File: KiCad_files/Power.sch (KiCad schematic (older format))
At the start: 101 parts, among them J2 PCIe_6_Pin_Power, Q1 Q_NMOS_DGS, Q2 Q_PMOS_DGS, U1 XC7A35T_CSG325, U13 LM2676, U2 MAX15027, U3 PI3420, U4 PI3421, U5 PI3420

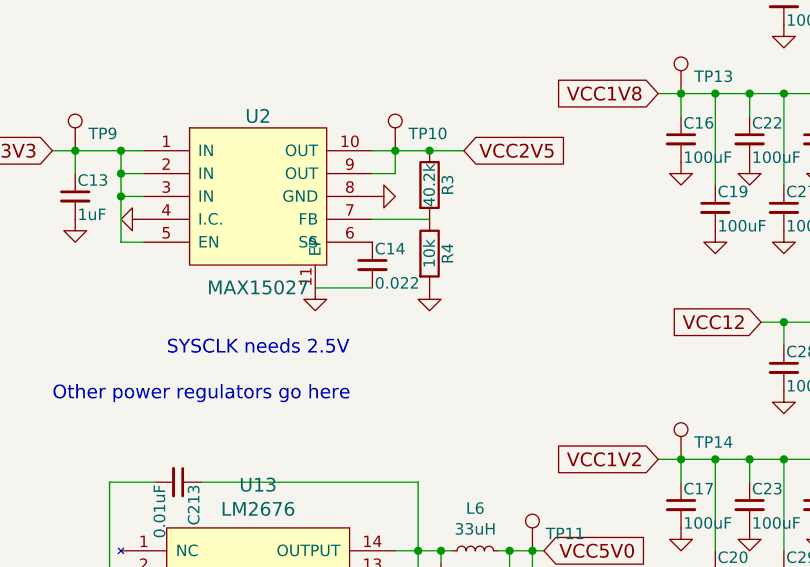
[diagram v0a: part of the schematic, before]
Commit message: Started mapping footprints
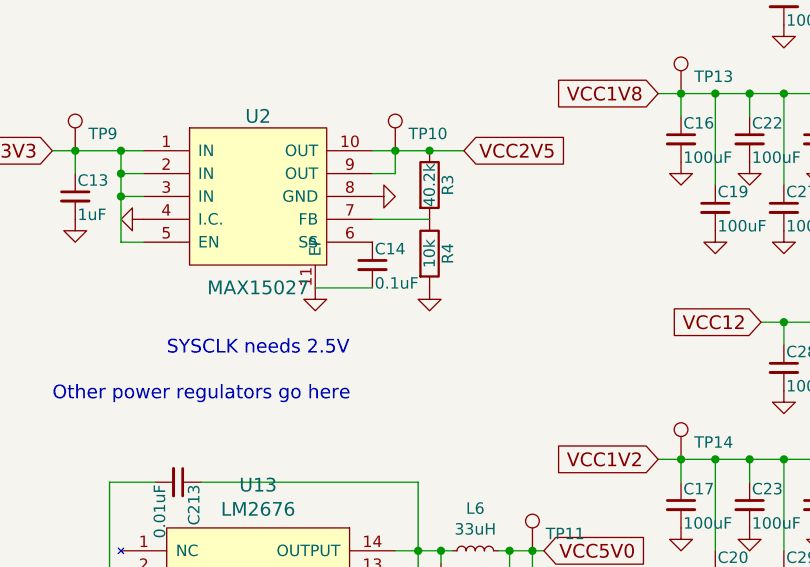
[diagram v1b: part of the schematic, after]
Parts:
- C11, C33, C35, C42, C43, C48, C49, C54, C56, C63, C64, C66, C67: footprint (none) -> Capacitors_SMD:C_0805
- C12, C15, C16, C17, C18, C19, C20, C21, C22, C23, C24, C25, C26, C27, C28, C29, C30, C31, C32, C34: footprint (none) -> Capacitors_SMD:C_1210
- C13: footprint (none) -> Capacitors_SMD:C_0402
- C14: value 0.022 -> 0.1uF; footprint (none) -> Capacitors_SMD:C_0402
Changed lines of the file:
@@
 F 0 "C11" H 2125 1350 50  0000 L CNN
 F 1 "10uF" H 2125 1150 50  0000 L CNN
-F 2 "" H 2138 1100 50  0001 C CNN
+F 2 "Capacitors_SMD:C_0805" H 2138 1100 50  0001 C CNN
 F 3 "" H 2100 1250 50  0001 C CNN
 	1    2100 1250
@@
 F 0 "C12" H 2475 1350 50  0000 L CNN
 F 1 "330uF" H 2475 1150 50  0000 L CNN
-F 2 "" H 2450 1250 50  0001 C CNN
+F 2 "Capacitors_SMD:C_1210" H 2450 1250 50  0001 C CNN
 F 3 "" H 2450 1250 50  0001 C CNN
 	1    2450 1250
@@
 F 0 "C15" H 6760 1870 50  0000 L CNN
 F 1 "100uF" H 6760 1720 50  0000 L CNN
-F 2 "" H 6750 1800 50  0001 C CNN
+F 2 "Capacitors_SMD:C_1210" H 6750 1800 50  0001 C CNN
 F 3 "" H 6750 1800 50  0001 C CNN
 	1    6750 1800
@@
 F 0 "C24" H 7210 1270 50  0000 L CNN
 F 1 "100uF" H 7210 1120 50  0000 L CNN
-F 2 "" H 7200 1200 50  0001 C CNN
+F 2 "Capacitors_SMD:C_1210" H 7200 1200 50  0001 C CNN
 F 3 "" H 7200 1200 50  0001 C CNN
 	1    7200 1200
@@
 F 0 "C33" H 7510 1270 50  0000 L CNN
 F 1 "22uF" H 7510 1120 50  0000 L CNN
-F 2 "" H 7500 1200 50  0001 C CNN
+F 2 "Capacitors_SMD:C_0805" H 7500 1200 50  0001 C CNN
 F 3 "" H 7500 1200 50  0001 C CNN
 	1    7500 1200
@@
 F 0 "C42" H 7710 1270 50  0000 L CNN
 F 1 "22uF" H 7710 1120 50  0000 L CNN
-F 2 "" H 7700 1200 50  0001 C CNN
+F 2 "Capacitors_SMD:C_0805" H 7700 1200 50  0001 C CNN
 F 3 "" H 7700 1200 50  0001 C CNN
 	1    7700 1200
@@
 F 0 "C48" H 7910 1270 50  0000 L CNN
 F 1 "22uF" H 7910 1120 50  0000 L CNN
-F 2 "" H 7900 1200 50  0001 C CNN
+F 2 "Capacitors_SMD:C_0805" H 7900 1200 50  0001 C CNN
 F 3 "" H 7900 1200 50  0001 C CNN
 	1    7900 1200
@@
 F 0 "C54" H 8110 1270 50  0000 L CNN
 F 1 "22uF" H 8110 1120 50  0000 L CNN
-F 2 "" H 8100 1200 50  0001 C CNN
+F 2 "Capacitors_SMD:C_0805" H 8100 1200 50  0001 C CNN
 F 3 "" H 8100 1200 50  0001 C CNN
 	1    8100 1200
@@
 F 0 "C63" H 8310 1270 50  0000 L CNN
 F 1 "22uF" H 8310 1120 50  0000 L CNN
-F 2 "" H 8300 1200 50  0001 C CNN
+F 2 "Capacitors_SMD:C_0805" H 8300 1200 50  0001 C CNN
 F 3 "" H 8300 1200 50  0001 C CNN
 	1    8300 1200
@@
 F 0 "C66" H 8510 1270 50  0000 L CNN
 F 1 "22uF" H 8510 1120 50  0000 L CNN
-F 2 "" H 8500 1200 50  0001 C CNN
+F 2 "Capacitors_SMD:C_0805" H 8500 1200 50  0001 C CNN
 F 3 "" H 8500 1200 50  0001 C CNN
 	1    8500 1200
@@
 F 0 "C18" H 6910 2170 50  0000 L CNN
 F 1 "100uF" H 6910 2020 50  0000 L CNN
-F 2 "" H 6900 2100 50  0001 C CNN
+F 2 "Capacitors_SMD:C_1210" H 6900 2100 50  0001 C CNN
 F 3 "" H 6900 2100 50  0001 C CNN
 	1    6900 2100
@@
 F 0 "C21" H 7060 1870 50  0000 L CNN
 F 1 "100uF" H 7060 1720 50  0000 L CNN
-F 2 "" H 7050 1800 50  0001 C CNN
+F 2 "Capacitors_SMD:C_1210" H 7050 1800 50  0001 C CNN
 F 3 "" H 7050 1800 50  0001 C CNN
 	1    7050 1800
@@
 F 0 "C25" H 7210 2170 50  0000 L CNN
 F 1 "100uF" H 7210 2020 50  0000 L CNN
-F 2 "" H 7200 2100 50  0001 C CNN
+F 2 "Capacitors_SMD:C_1210" H 7200 2100 50  0001 C CNN
 F 3 "" H 7200 2100 50  0001 C CNN
 	1    7200 2100
@@
 F 0 "C30" H 7360 1870 50  0000 L CNN
 F 1 "100uF" H 7360 1720 50  0000 L CNN
-F 2 "" H 7350 1800 50  0001 C CNN
+F 2 "Capacitors_SMD:C_1210" H 7350 1800 50  0001 C CNN
 F 3 "" H 7350 1800 50  0001 C CNN
 	1    7350 1800
@@
 F 0 "C34" H 7510 2170 50  0000 L CNN
 F 1 "100uF" H 7510 2020 50  0000 L CNN
-F 2 "" H 7500 2100 50  0001 C CNN
+F 2 "Capacitors_SMD:C_1210" H 7500 2100 50  0001 C CNN
 F 3 "" H 7500 2100 50  0001 C CNN
 	1    7500 2100
@@
 F 0 "C16" H 6760 3470 50  0000 L CNN
 F 1 "100uF" H 6760 3320 50  0000 L CNN
-F 2 "" H 6750 3400 50  0001 C CNN
+F 2 "Capacitors_SMD:C_1210" H 6750 3400 50  0001 C CNN
 F 3 "" H 6750 3400 50  0001 C CNN
 	1    6750 3400
@@
 F 0 "C26" H 7210 2870 50  0000 L CNN
 F 1 "100uF" H 7210 2720 50  0000 L CNN
-F 2 "" H 7200 2800 50  0001 C CNN
+F 2 "Capacitors_SMD:C_1210" H 7200 2800 50  0001 C CNN
 F 3 "" H 7200 2800 50  0001 C CNN
 	1    7200 2800
@@
 F 0 "C35" H 7510 2870 50  0000 L CNN
 F 1 "22uF" H 7510 2720 50  0000 L CNN
-F 2 "" H 7500 2800 50  0001 C CNN
+F 2 "Capacitors_SMD:C_0805" H 7500 2800 50  0001 C CNN
 F 3 "" H 7500 2800 50  0001 C CNN
 	1    7500 2800
@@
 F 0 "C43" H 7710 2870 50  0000 L CNN
 F 1 "22uF" H 7710 2720 50  0000 L CNN
-F 2 "" H 7700 2800 50  0001 C CNN
+F 2 "Capacitors_SMD:C_0805" H 7700 2800 50  0001 C CNN
 F 3 "" H 7700 2800 50  0001 C CNN
 	1    7700 2800
@@
 F 0 "C49" H 7910 2870 50  0000 L CNN
 F 1 "22uF" H 7910 2720 50  0000 L CNN
-F 2 "" H 7900 2800 50  0001 C CNN
+F 2 "Capacitors_SMD:C_0805" H 7900 2800 50  0001 C CNN
 F 3 "" H 7900 2800 50  0001 C CNN
 	1    7900 2800
@@
 F 0 "C56" H 8110 2870 50  0000 L CNN
 F 1 "22uF" H 8110 2720 50  0000 L CNN
-F 2 "" H 8100 2800 50  0001 C CNN
+F 2 "Capacitors_SMD:C_0805" H 8100 2800 50  0001 C CNN
 F 3 "" H 8100 2800 50  0001 C CNN
 	1    8100 2800
@@
 F 0 "C64" H 8310 2870 50  0000 L CNN
 F 1 "22uF" H 8310 2720 50  0000 L CNN
-F 2 "" H 8300 2800 50  0001 C CNN
+F 2 "Capacitors_SMD:C_0805" H 8300 2800 50  0001 C CNN
 F 3 "" H 8300 2800 50  0001 C CNN
 	1    8300 2800
@@
 F 0 "C67" H 8510 2870 50  0000 L CNN
 F 1 "22uF" H 8510 2720 50  0000 L CNN
-F 2 "" H 8500 2800 50  0001 C CNN
+F 2 "Capacitors_SMD:C_0805" H 8500 2800 50  0001 C CNN
 F 3 "" H 8500 2800 50  0001 C CNN
 	1    8500 2800
@@
 F 0 "C19" H 6910 3770 50  0000 L CNN
 F 1 "100uF" H 6910 3620 50  0000 L CNN
-F 2 "" H 6900 3700 50  0001 C CNN
+F 2 "Capacitors_SMD:C_1210" H 6900 3700 50  0001 C CNN
 F 3 "" H 6900 3700 50  0001 C CNN
 	1    6900 3700
@@
 F 0 "C22" H 7060 3470 50  0000 L CNN
 F 1 "100uF" H 7060 3320 50  0000 L CNN
-F 2 "" H 7050 3400 50  0001 C CNN
+F 2 "Capacitors_SMD:C_1210" H 7050 3400 50  0001 C CNN
 F 3 "" H 7050 3400 50  0001 C CNN
 	1    7050 3400
@@
 F 0 "C27" H 7210 3770 50  0000 L CNN
 F 1 "100uF" H 7210 3620 50  0000 L CNN
-F 2 "" H 7200 3700 50  0001 C CNN
+F 2 "Capacitors_SMD:C_1210" H 7200 3700 50  0001 C CNN
 F 3 "" H 7200 3700 50  0001 C CNN
 	1    7200 3700
@@
 F 0 "C31" H 7360 3470 50  0000 L CNN
 F 1 "100uF" H 7360 3320 50  0000 L CNN
-F 2 "" H 7350 3400 50  0001 C CNN
+F 2 "Capacitors_SMD:C_1210" H 7350 3400 50  0001 C CNN
 F 3 "" H 7350 3400 50  0001 C CNN
 	1    7350 3400
@@
 F 0 "C17" H 6760 5070 50  0000 L CNN
 F 1 "100uF" H 6760 4920 50  0000 L CNN
-F 2 "" H 6750 5000 50  0001 C CNN
+F 2 "Capacitors_SMD:C_1210" H 6750 5000 50  0001 C CNN
 F 3 "" H 6750 5000 50  0001 C CNN
 	1    6750 5000
@@
 F 0 "C28" H 7210 4470 50  0000 L CNN
 F 1 "100uF" H 7210 4320 50  0000 L CNN
-F 2 "" H 7200 4400 50  0001 C CNN
+F 2 "Capacitors_SMD:C_1210" H 7200 4400 50  0001 C CNN
 F 3 "" H 7200 4400 50  0001 C CNN
 	1    7200 4400
@@
 F 0 "C20" H 6910 5370 50  0000 L CNN
 F 1 "100uF" H 6910 5220 50  0000 L CNN
-F 2 "" H 6900 5300 50  0001 C CNN
+F 2 "Capacitors_SMD:C_1210" H 6900 5300 50  0001 C CNN
 F 3 "" H 6900 5300 50  0001 C CNN
 	1    6900 5300
@@
 F 0 "C23" H 7060 5070 50  0000 L CNN
 F 1 "100uF" H 7060 4920 50  0000 L CNN
-F 2 "" H 7050 5000 50  0001 C CNN
+F 2 "Capacitors_SMD:C_1210" H 7050 5000 50  0001 C CNN
 F 3 "" H 7050 5000 50  0001 C CNN
 	1    7050 5000
@@
 F 0 "C29" H 7210 5370 50  0000 L CNN
 F 1 "100uF" H 7210 5220 50  0000 L CNN
-F 2 "" H 7200 5300 50  0001 C CNN
+F 2 "Capacitors_SMD:C_1210" H 7200 5300 50  0001 C CNN
 F 3 "" H 7200 5300 50  0001 C CNN
 	1    7200 5300
@@
 F 0 "C32" H 7360 5070 50  0000 L CNN
 F 1 "100uF" H 7360 4920 50  0000 L CNN
-F 2 "" H 7350 5000 50  0001 C CNN
+F 2 "Capacitors_SMD:C_1210" H 7350 5000 50  0001 C CNN
 F 3 "" H 7350 5000 50  0001 C CNN
 	1    7350 5000
@@
 F 0 "C13" H 4110 3720 50  0000 L CNN
 F 1 "1uF" H 4110 3570 50  0000 L CNN
-F 2 "" H 4100 3650 50  0001 C CNN
+F 2 "Capacitors_SMD:C_0402" H 4100 3650 50  0001 C CNN
 F 3 "" H 4100 3650 50  0001 C CNN
 	1    4100 3650
@@
 P 5400 3950
 F 0 "C14" H 5410 4020 50  0000 L CNN
-F 1 "0.022" H 5410 3870 50  0000 L CNN
-F 2 "" H 5400 3950 50  0001 C CNN
+F 1 "0.1uF" H 5410 3870 50  0000 L CNN
+F 2 "Capacitors_SMD:C_0402" H 5400 3950 50  0001 C CNN
 F 3 "" H 5400 3950 50  0001 C CNN
 	1    5400 3950

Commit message: Finished capacitor footprints
Total cost: ~$55
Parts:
- C210, C211, C36, C38, C39, C40, C41, C45, C46, C47: footprint (none) -> Capacitors_SMD:C_1210
- C212, C51, C52, C53, C55, C57, C59: footprint (none) -> Capacitors_SMD:C_0402
- C213, C60, C61, C62: footprint (none) -> Capacitors_SMD:C_0201
- C218: footprint (none) -> Capacitors_SMD:C_1206
- C37, C44, C50, C58, C65, C68: footprint (none) -> Capacitors_SMD:C_0805
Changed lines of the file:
@@
 F 0 "C51" H 7960 1870 50  0000 L CNN
 F 1 "1uF" H 7960 1720 50  0000 L CNN
-F 2 "" H 7950 1800 50  0001 C CNN
+F 2 "Capacitors_SMD:C_0402" H 7950 1800 50  0001 C CNN
 F 3 "" H 7950 1800 50  0001 C CNN
 	1    7950 1800
@@
 F 0 "C55" H 8110 1870 50  0000 L CNN
 F 1 "1uF" H 8110 1720 50  0000 L CNN
-F 2 "" H 8100 1800 50  0001 C CNN
+F 2 "Capacitors_SMD:C_0402" H 8100 1800 50  0001 C CNN
 F 3 "" H 8100 1800 50  0001 C CNN
 	1    8100 1800
@@
 F 0 "C39" H 7660 1870 50  0000 L CNN
 F 1 "100uF" H 7660 1720 50  0000 L CNN
-F 2 "" H 7650 1800 50  0001 C CNN
+F 2 "Capacitors_SMD:C_1210" H 7650 1800 50  0001 C CNN
 F 3 "" H 7650 1800 50  0001 C CNN
 	1    7650 1800
@@
 F 0 "C45" H 7810 2170 50  0000 L CNN
 F 1 "100uF" H 7810 2020 50  0000 L CNN
-F 2 "" H 7800 2100 50  0001 C CNN
+F 2 "Capacitors_SMD:C_1210" H 7800 2100 50  0001 C CNN
 F 3 "" H 7800 2100 50  0001 C CNN
 	1    7800 2100
@@
 F 0 "C60" H 8260 1870 50  0000 L CNN
 F 1 "0.1uF" H 8260 1720 50  0000 L CNN
-F 2 "" H 8250 1800 50  0001 C CNN
+F 2 "Capacitors_SMD:C_0201" H 8250 1800 50  0001 C CNN
 F 3 "" H 8250 1800 50  0001 C CNN
 	1    8250 1800
@@
 F 0 "C36" H 7510 3770 50  0000 L CNN
 F 1 "100uF" H 7510 3620 50  0000 L CNN
-F 2 "" H 7500 3700 50  0001 C CNN
+F 2 "Capacitors_SMD:C_1210" H 7500 3700 50  0001 C CNN
 F 3 "" H 7500 3700 50  0001 C CNN
 	1    7500 3700
@@
 F 0 "C52" H 7960 3470 50  0000 L CNN
 F 1 "1uF" H 7960 3320 50  0000 L CNN
-F 2 "" H 7950 3400 50  0001 C CNN
+F 2 "Capacitors_SMD:C_0402" H 7950 3400 50  0001 C CNN
 F 3 "" H 7950 3400 50  0001 C CNN
 	1    7950 3400
@@
 F 0 "C57" H 8110 3470 50  0000 L CNN
 F 1 "1uF" H 8110 3320 50  0000 L CNN
-F 2 "" H 8100 3400 50  0001 C CNN
+F 2 "Capacitors_SMD:C_0402" H 8100 3400 50  0001 C CNN
 F 3 "" H 8100 3400 50  0001 C CNN
 	1    8100 3400
@@
 F 0 "C40" H 7660 3470 50  0000 L CNN
 F 1 "100uF" H 7660 3320 50  0000 L CNN
-F 2 "" H 7650 3400 50  0001 C CNN
+F 2 "Capacitors_SMD:C_1210" H 7650 3400 50  0001 C CNN
 F 3 "" H 7650 3400 50  0001 C CNN
 	1    7650 3400
@@
 F 0 "C46" H 7810 3770 50  0000 L CNN
 F 1 "100uF" H 7810 3620 50  0000 L CNN
-F 2 "" H 7800 3700 50  0001 C CNN
+F 2 "Capacitors_SMD:C_1210" H 7800 3700 50  0001 C CNN
 F 3 "" H 7800 3700 50  0001 C CNN
 	1    7800 3700
@@
 F 0 "C61" H 8260 3470 50  0000 L CNN
 F 1 "0.1uF" H 8260 3320 50  0000 L CNN
-F 2 "" H 8250 3400 50  0001 C CNN
+F 2 "Capacitors_SMD:C_0201" H 8250 3400 50  0001 C CNN
 F 3 "" H 8250 3400 50  0001 C CNN
 	1    8250 3400
@@
 F 0 "C37" H 7510 4470 50  0000 L CNN
 F 1 "22uF" H 7510 4320 50  0000 L CNN
-F 2 "" H 7500 4400 50  0001 C CNN
+F 2 "Capacitors_SMD:C_0805" H 7500 4400 50  0001 C CNN
 F 3 "" H 7500 4400 50  0001 C CNN
 	1    7500 4400
@@
 F 0 "C44" H 7710 4470 50  0000 L CNN
 F 1 "22uF" H 7710 4320 50  0000 L CNN
-F 2 "" H 7700 4400 50  0001 C CNN
+F 2 "Capacitors_SMD:C_0805" H 7700 4400 50  0001 C CNN
 F 3 "" H 7700 4400 50  0001 C CNN
 	1    7700 4400
@@
 F 0 "C50" H 7910 4470 50  0000 L CNN
 F 1 "22uF" H 7910 4320 50  0000 L CNN
-F 2 "" H 7900 4400 50  0001 C CNN
+F 2 "Capacitors_SMD:C_0805" H 7900 4400 50  0001 C CNN
 F 3 "" H 7900 4400 50  0001 C CNN
 	1    7900 4400
@@
 F 0 "C58" H 8110 4470 50  0000 L CNN
 F 1 "22uF" H 8110 4320 50  0000 L CNN
-F 2 "" H 8100 4400 50  0001 C CNN
+F 2 "Capacitors_SMD:C_0805" H 8100 4400 50  0001 C CNN
 F 3 "" H 8100 4400 50  0001 C CNN
 	1    8100 4400
@@
 F 0 "C65" H 8310 4470 50  0000 L CNN
 F 1 "22uF" H 8310 4320 50  0000 L CNN
-F 2 "" H 8300 4400 50  0001 C CNN
+F 2 "Capacitors_SMD:C_0805" H 8300 4400 50  0001 C CNN
 F 3 "" H 8300 4400 50  0001 C CNN
 	1    8300 4400
@@
 F 0 "C68" H 8510 4470 50  0000 L CNN
 F 1 "22uF" H 8510 4320 50  0000 L CNN
-F 2 "" H 8500 4400 50  0001 C CNN
+F 2 "Capacitors_SMD:C_0805" H 8500 4400 50  0001 C CNN
 F 3 "" H 8500 4400 50  0001 C CNN
 	1    8500 4400
@@
 F 0 "C38" H 7510 5370 50  0000 L CNN
 F 1 "100uF" H 7510 5220 50  0000 L CNN
-F 2 "" H 7500 5300 50  0001 C CNN
+F 2 "Capacitors_SMD:C_1210" H 7500 5300 50  0001 C CNN
 F 3 "" H 7500 5300 50  0001 C CNN
 	1    7500 5300
@@
 F 0 "C53" H 7960 5070 50  0000 L CNN
 F 1 "1uF" H 7960 4920 50  0000 L CNN
-F 2 "" H 7950 5000 50  0001 C CNN
+F 2 "Capacitors_SMD:C_0402" H 7950 5000 50  0001 C CNN
 F 3 "" H 7950 5000 50  0001 C CNN
 	1    7950 5000
@@
 F 0 "C59" H 8110 5070 50  0000 L CNN
 F 1 "1uF" H 8110 4920 50  0000 L CNN
-F 2 "" H 8100 5000 50  0001 C CNN
+F 2 "Capacitors_SMD:C_0402" H 8100 5000 50  0001 C CNN
 F 3 "" H 8100 5000 50  0001 C CNN
 	1    8100 5000
@@
 F 0 "C41" H 7660 5070 50  0000 L CNN
 F 1 "100uF" H 7660 4920 50  0000 L CNN
-F 2 "" H 7650 5000 50  0001 C CNN
+F 2 "Capacitors_SMD:C_1210" H 7650 5000 50  0001 C CNN
 F 3 "" H 7650 5000 50  0001 C CNN
 	1    7650 5000
@@
 F 0 "C47" H 7810 5370 50  0000 L CNN
 F 1 "100uF" H 7810 5220 50  0000 L CNN
-F 2 "" H 7800 5300 50  0001 C CNN
+F 2 "Capacitors_SMD:C_1210" H 7800 5300 50  0001 C CNN
 F 3 "" H 7800 5300 50  0001 C CNN
 	1    7800 5300
@@
 F 0 "C62" H 8260 5070 50  0000 L CNN
 F 1 "0.1uF" H 8260 4920 50  0000 L CNN
-F 2 "" H 8250 5000 50  0001 C CNN
+F 2 "Capacitors_SMD:C_0201" H 8250 5000 50  0001 C CNN
 F 3 "" H 8250 5000 50  0001 C CNN
 	1    8250 5000
@@
 F 0 "C210" H 3810 5520 50  0000 L CNN
 F 1 "15uF" H 3810 5370 50  0000 L CNN
-F 2 "" H 3800 5450 50  0001 C CNN
+F 2 "Capacitors_SMD:C_1210" H 3800 5450 50  0001 C CNN
 F 3 "" H 3800 5450 50  0001 C CNN
 	1    3800 5450
@@
 F 0 "C211" H 4010 5520 50  0000 L CNN
 F 1 "15uF" H 4010 5370 50  0000 L CNN
-F 2 "" H 4000 5450 50  0001 C CNN
+F 2 "Capacitors_SMD:C_1210" H 4000 5450 50  0001 C CNN
 F 3 "" H 4000 5450 50  0001 C CNN
 	1    4000 5450
@@
 F 0 "C212" H 4210 6170 50  0000 L CNN
 F 1 "0.47uF" H 4210 6020 50  0000 L CNN
-F 2 "" H 4200 6100 50  0001 C CNN
+F 2 "Capacitors_SMD:C_0402" H 4200 6100 50  0001 C CNN
 F 3 "" H 4200 6100 50  0001 C CNN
 	1    4200 6100
@@
 F 0 "C213" H 4560 4970 50  0000 L CNN
 F 1 "0.01uF" H 4560 4820 50  0000 L CNN
-F 2 "" H 4550 4900 50  0001 C CNN
+F 2 "Capacitors_SMD:C_0201" H 4550 4900 50  0001 C CNN
 F 3 "" H 4550 4900 50  0001 C CNN
 	1    4550 4900
@@
 F 0 "C218" H 6010 5470 50  0000 L CNN
 F 1 "180uF" H 6010 5320 50  0000 L CNN
-F 2 "" H 6000 5400 50  0001 C CNN
+F 2 "Capacitors_SMD:C_1206" H 6000 5400 50  0001 C CNN
 F 3 "" H 6000 5400 50  0001 C CNN
 	1    6000 5400
